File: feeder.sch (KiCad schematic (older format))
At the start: 10 parts, among them J5 Feeder, J6 Chain

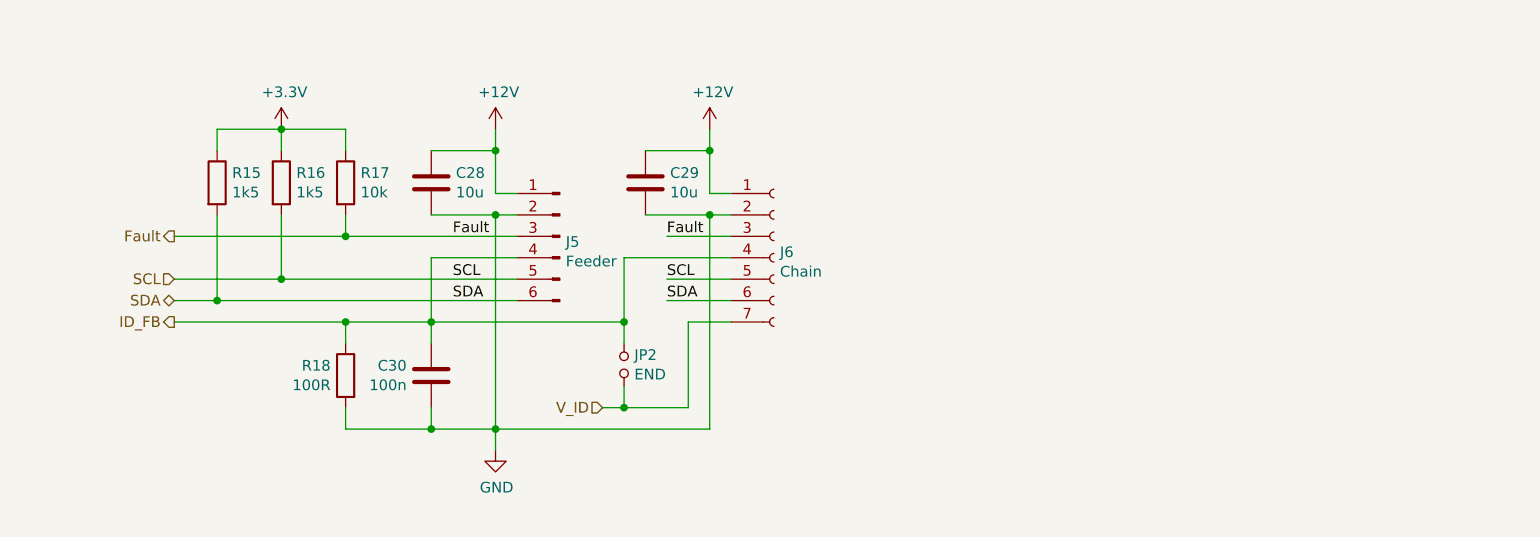
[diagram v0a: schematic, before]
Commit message: Added IO Protection Switched Fault Signal to +3.3V Added Voltage sensing Added correct UART pins to EXT header
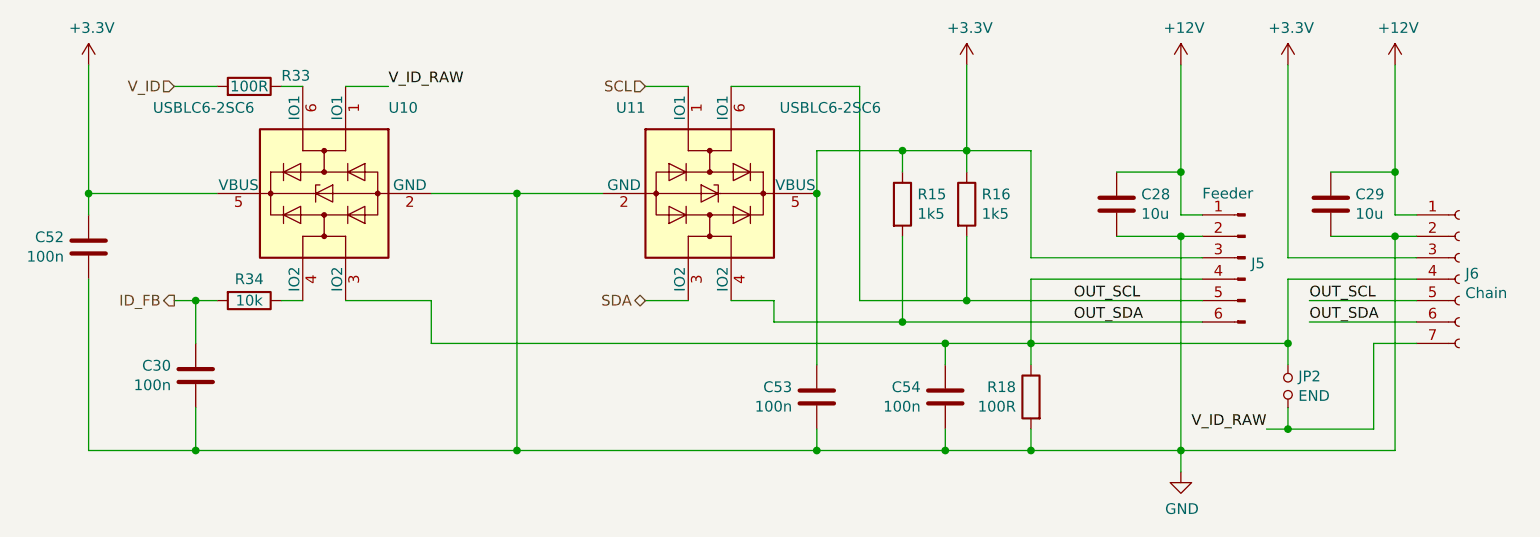
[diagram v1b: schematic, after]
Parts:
- removed R17: 10k, Resistor_SMD:R_0603_1608Metric, symbol Device:R
- added C52, C53, C54: 100n, Capacitor_SMD:C_0603_1608Metric, symbol Device:C
- added R33: 100R, Resistor_SMD:R_0603_1608Metric, symbol Device:R
- added R34: 10k, Resistor_SMD:R_0603_1608Metric, symbol Device:R
- added U10, U11: USBLC6-2SC6, Package_TO_SOT_SMD:SOT-23-6, symbol Power_Protection:USBLC6-2SC6
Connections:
- net Fault is gone; now on net +3V3: J5.3 (Pin_3), J6.3 (Pin_3)
- net +3V3: now also C52.1, C53.1, U10.5 (VBUS), U11.5 (VBUS)
- net GND: now also C52.2, C53.2, C54.2, U10.2 (GND), U11.2 (GND)
- net ID_FB: now also R34.2; no longer J5.4 (Pin_4), J6.4 (Pin_4), JP2.1, R18.1
- net SCL: now also U11.1 (IO1); no longer J5.5 (Pin_5), J6.5 (Pin_5), R16.2
- net SDA: now also U11.3 (IO2); no longer J5.6 (Pin_6), J6.6 (Pin_6), R15.2
- net V_ID: now also R33.2; no longer J6.7 (Pin_7), JP2.2
- new net: C54.1, J5.4 (Pin_4), J6.4 (Pin_4), JP2.1, R18.1, U10.3 (IO2)
- new net: R34.1, U10.4 (IO2)
- new net: R33.1, U10.6 (IO1)
- new net OUT_SCL: J5.5 (Pin_5), J6.5 (Pin_5), R16.2, U11.6 (IO1)
- new net OUT_SDA: J5.6 (Pin_6), J6.6 (Pin_6), R15.2, U11.4 (IO2)
- new net V_ID_RAW: J6.7 (Pin_7), JP2.2, U10.1 (IO1)
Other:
- moved on the sheet: C28, C29, C30, J5, J6, JP2, R15, R16, R18
